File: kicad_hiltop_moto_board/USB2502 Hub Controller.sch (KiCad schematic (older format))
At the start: 39 parts, among them U27 USB2502, U7 AT24C02C-SSHM-T, Y1 50ppm 24.000MHZ

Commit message: Unused pind removed from moto board
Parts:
- U27: symbol Motor_Control_Board-rescue:USB2502-Devtank-Sensi_Board-rescue -> moto_board-rescue:USB2502-Devtank-Sensi_Board-rescue-Motor_Control_Board-rescue
- U7: symbol Motor_Control_Board-rescue:AT24C02C-SSHM-T-Devtank-Sensi_Board-rescue -> moto_board-rescue:AT24C02C-SSHM-T-Devtank-Sensi_Board-rescue-Motor_Control_Board-rescue
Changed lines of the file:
@@
 EESchema Schematic File Version 4
-LIBS:Motor_Control_Board-cache
+LIBS:moto_board-cache
 EELAYER 30 0
 EELAYER END
@@
 $EndDescr
 $Comp
-L Motor_Control_Board-rescue:USB2502-Devtank-Sensi_Board-rescue U27
+L moto_board-rescue:USB2502-Devtank-Sensi_Board-rescue-Motor_Control_Board-rescue U27
 U 1 1 5D8D0F87
 P 6150 4500
@@
 NoConn ~ 5150 3600
 $Comp
-L Motor_Control_Board-rescue:AT24C02C-SSHM-T-Devtank-Sensi_Board-rescue U7
+L moto_board-rescue:AT24C02C-SSHM-T-Devtank-Sensi_Board-rescue-Motor_Control_Board-rescue U7
 U 1 1 5D7EF6D2
 P 9350 5700
+AR Path="/5D7EF6D2" Ref="U7"  Part="1"
+AR Path="/5D8D08E6/5D7EF6D2" Ref="U7"  Part="1"
 F 0 "U7" H 9375 6187 60  0000 C CNN
 F 1 "AT24C02C-SSHM-T" H 9375 6081 60  0000 C CNN

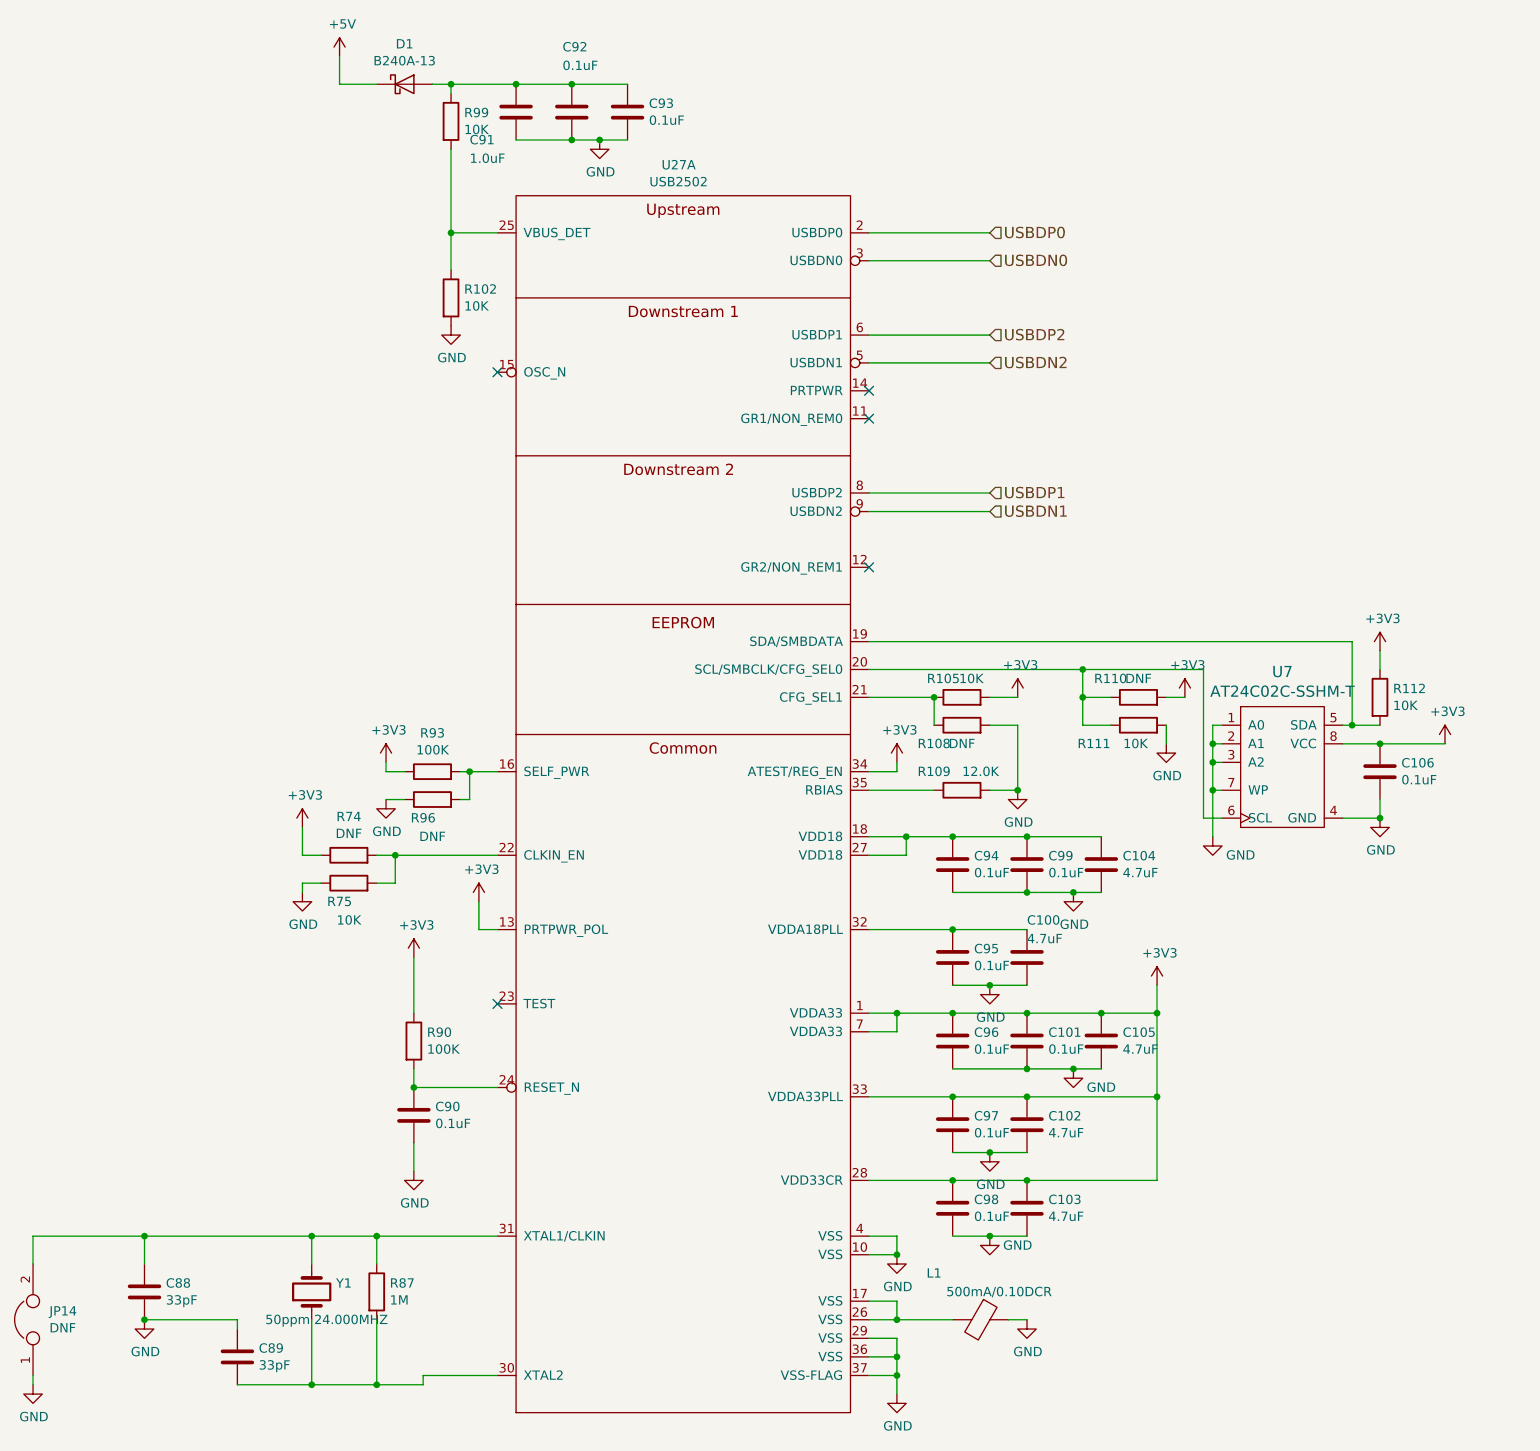
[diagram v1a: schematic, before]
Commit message: Rough layout of moto board
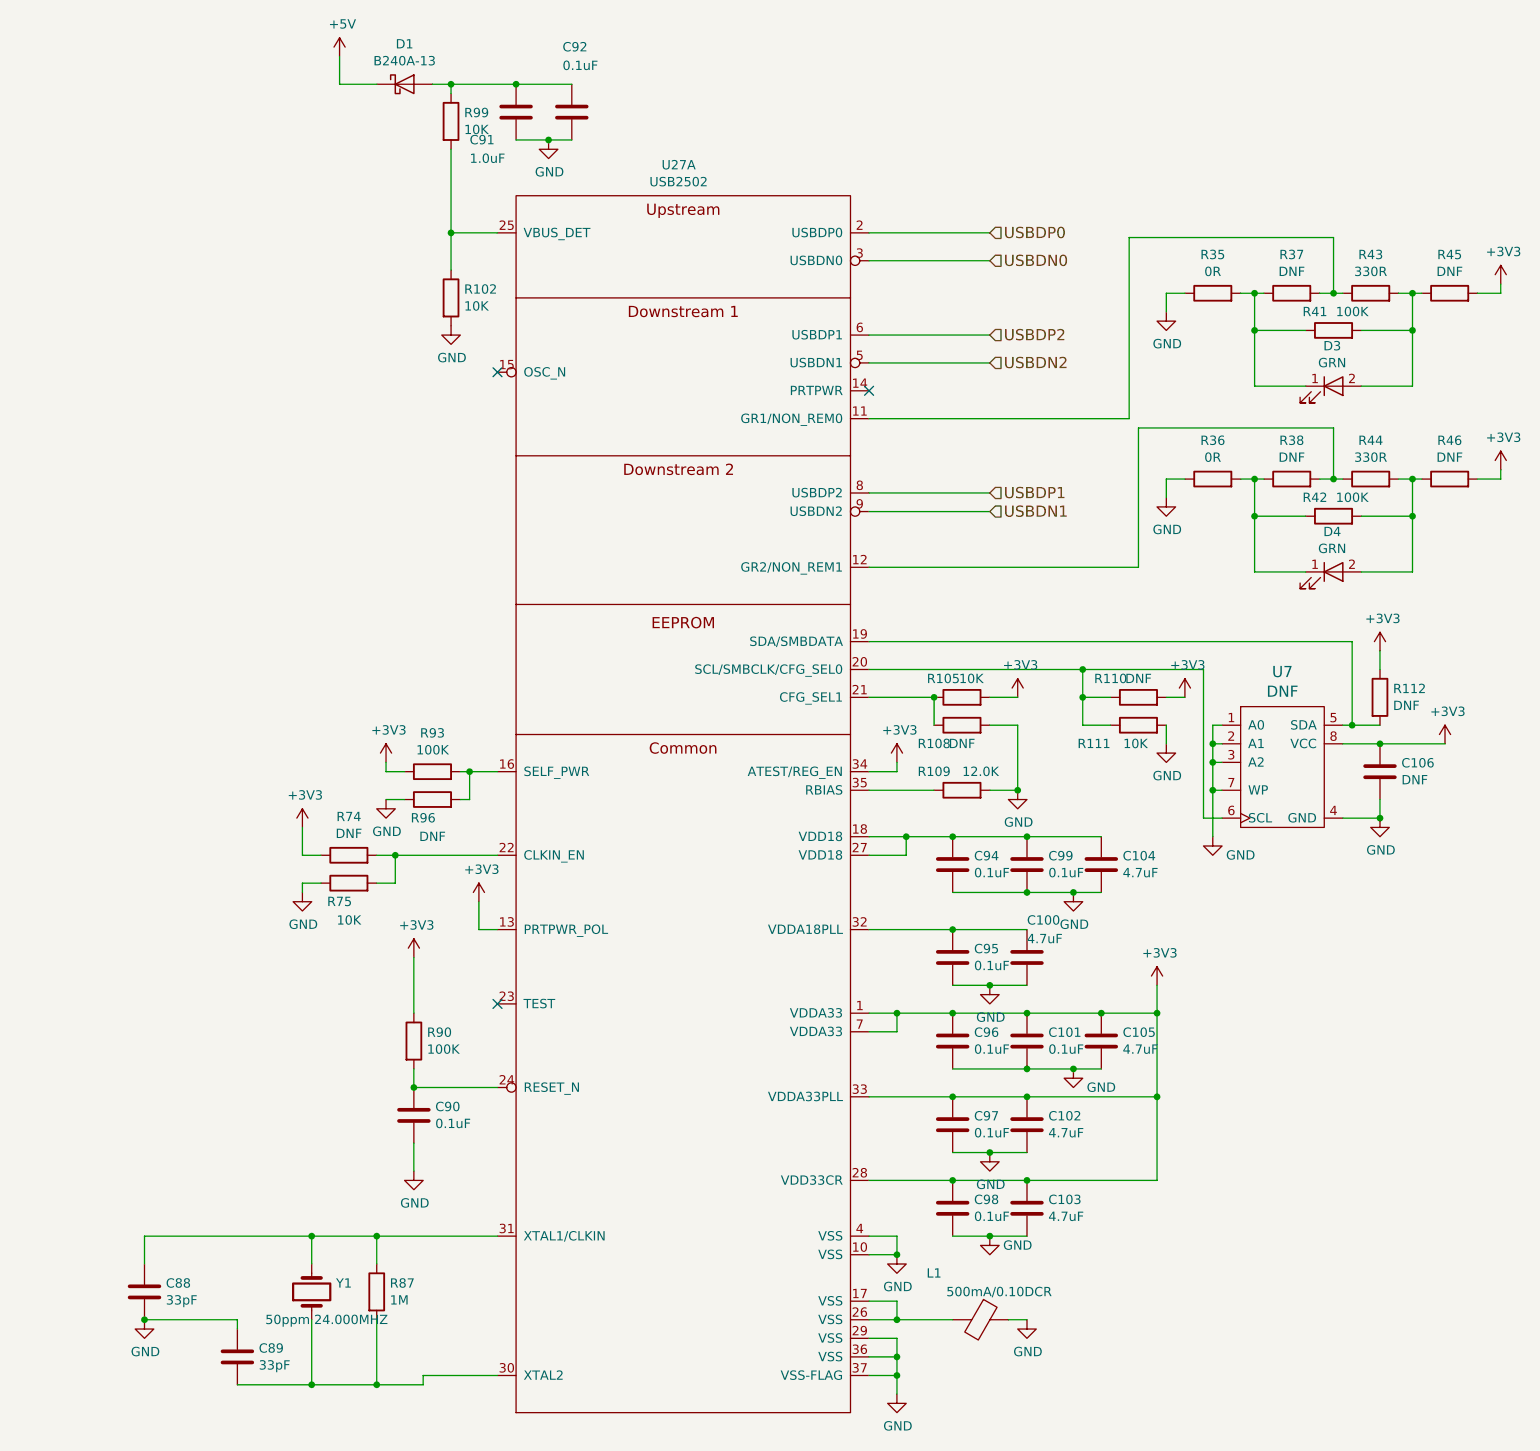
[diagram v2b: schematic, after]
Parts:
- removed C93: 0.1uF, Capacitor_SMD:C_0402_1005Metric, symbol device:C
- removed JP14: DNF, Connector_PinHeader_2.54mm:PinHeader_1x02_P2.54mm_Vertical, symbol device:Jumper
- added D3, D4: GRN, LED_SMD:LED_0603_1608Metric, symbol device:LED
- added R35, R36: 0R, Resistor_SMD:R_0603_1608Metric, symbol device:R
- added R37, R38, R45, R46: DNF, Resistor_SMD:R_0603_1608Metric, symbol device:R
- added R41, R42: 100K, Resistor_SMD:R_0603_1608Metric, symbol device:R
- added R43, R44: 330R, Resistor_SMD:R_0603_1608Metric, symbol device:R
- C106: value 0.1uF -> DNF
- R112: value 10K -> DNF
- U7: value AT24C02C-SSHM-T -> DNF
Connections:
- net +3V3: now also R45.2, R46.2
- net GND: now also R35.1, R36.1
- net at U27.11 (GR1/NON_REM0): now also R37.2, R43.1
- net at U27.12 (GR2/NON_REM1): now also R38.2, R44.1
- new net: D4.1 (K), R36.2, R38.1, R42.1
- new net: D4.2 (A), R42.2, R44.2, R46.1
- new net: D3.1 (K), R35.2, R37.1, R41.1
- new net: D3.2 (A), R41.2, R43.2, R45.1
- no-connect marks 5 -> 3

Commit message: Moto board awaiting review
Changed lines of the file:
@@
 P 4150 8550
 F 0 "Y1" V 4196 8419 50  0000 R CNN
-F 1 "50ppm 24.000MHZ" V 4000 8800 50  0000 R CNN
+F 1 "50ppm 24.000MHZ" V 3975 8900 50  0000 R CNN
 F 2 "Crystal:Crystal_SMD_TXC_7A-2Pin_5x3.2mm" H 4150 8550 50  0001 C CNN
 F 3 "" H 4150 8550 50  0001 C CNN
@@
 U 1 1 5D8F3D03
 P 7650 5500
-F 0 "R108" V 7550 5650 50  0000 C CNN
-F 1 "DNF" V 7550 5500 50  0000 C CNN
+F 0 "R108" V 7550 5600 50  0000 C CNN
+F 1 "DNF" V 7550 5375 50  0000 C CNN
 F 2 "Resistor_SMD:R_0603_1608Metric" V 7580 5500 50  0001 C CNN
 F 3 "" H 7650 5500 50  0001 C CNN
@@
 U 1 1 5D909BDF
 P 8000 7200
-F 0 "C101" H 8115 7246 50  0000 L CNN
-F 1 "0.1uF" H 8115 7155 50  0000 L CNN
+F 0 "C101" H 8100 7250 50  0000 L CNN
+F 1 "0.1uF" H 8100 7150 50  0000 L CNN
 F 2 "Capacitor_SMD:C_0402_1005Metric" H 8038 7050 50  0001 C CNN
 F 3 "" H 8000 7200 50  0001 C CNN
@@
 U 1 1 5D909BE5
 P 8400 7200
-F 0 "C105" H 8515 7246 50  0000 L CNN
-F 1 "4.7uF " H 8515 7155 50  0000 L CNN
+F 0 "C105" H 8500 7225 50  0000 L CNN
+F 1 "4.7uF " H 8475 7125 50  0000 L CNN
 F 2 "Capacitor_SMD:C_0402_1005Metric" H 8438 7050 50  0001 C CNN
 F 3 "" H 8400 7200 50  0001 C CNN
@@
 U 1 1 5D919F57
 P 7600 7650
-F 0 "C97" H 7715 7696 50  0000 L CNN
-F 1 "0.1uF" H 7715 7605 50  0000 L CNN
+F 0 "C97" H 7700 7675 50  0000 L CNN
+F 1 "0.1uF" H 7700 7600 50  0000 L CNN
 F 2 "Capacitor_SMD:C_0402_1005Metric" H 7638 7500 50  0001 C CNN
 F 3 "" H 7600 7650 50  0001 C CNN
@@
 U 1 1 5D929924
 P 7600 6750
-F 0 "C95" H 7715 6796 50  0000 L CNN
-F 1 "0.1uF" H 7715 6705 50  0000 L CNN
+F 0 "C95" H 7700 6800 50  0000 L CNN
+F 1 "0.1uF" H 7700 6700 50  0000 L CNN
 F 2 "Capacitor_SMD:C_0402_1005Metric" H 7638 6600 50  0001 C CNN
 F 3 "" H 7600 6750 50  0001 C CNN
@@
 U 1 1 5D92992A
 P 8000 6750
-F 0 "C100" H 8000 6950 50  0000 L CNN
-F 1 "4.7uF " H 8000 6850 50  0000 L CNN
+F 0 "C100" H 8125 6800 50  0000 L CNN
+F 1 "4.7uF " H 8125 6700 50  0000 L CNN
 F 2 "Capacitor_SMD:C_0402_1005Metric" H 8038 6600 50  0001 C CNN
 F 3 "" H 8000 6750 50  0001 C CNN
@@
 U 1 1 5D938ADF
 P 8000 6250
-F 0 "C99" H 8115 6296 50  0000 L CNN
-F 1 "0.1uF" H 8115 6205 50  0000 L CNN
+F 0 "C99" H 8100 6300 50  0000 L CNN
+F 1 "0.1uF" H 8100 6200 50  0000 L CNN
 F 2 "Capacitor_SMD:C_0402_1005Metric" H 8038 6100 50  0001 C CNN
 F 3 "" H 8000 6250 50  0001 C CNN
@@
 U 1 1 5D938AEB
 P 7600 6250
-F 0 "C94" H 7715 6296 50  0000 L CNN
-F 1 "0.1uF" H 7715 6205 50  0000 L CNN
+F 0 "C94" H 7700 6300 50  0000 L CNN
+F 1 "0.1uF" H 7700 6200 50  0000 L CNN
 F 2 "Capacitor_SMD:C_0402_1005Metric" H 7638 6100 50  0001 C CNN
 F 3 "" H 7600 6250 50  0001 C CNN
@@
 U 1 1 5D947DA8
 P 7650 5350
-F 0 "R105" V 7750 5450 50  0000 C CNN
-F 1 "10K" V 7750 5300 50  0000 C CNN
+F 0 "R105" V 7725 5450 50  0000 C CNN
+F 1 "10K" V 7725 5250 50  0000 C CNN
 F 2 "Resistor_SMD:R_0603_1608Metric" V 7580 5350 50  0001 C CNN
 F 3 "" H 7650 5350 50  0001 C CNN
@@
 U 1 1 5D949CAE
 P 8600 5350
-F 0 "R110" V 8700 5500 50  0000 C CNN
-F 1 "DNF" V 8700 5350 50  0000 C CNN
+F 0 "R110" V 8675 5475 50  0000 C CNN
+F 1 "DNF" V 8675 5250 50  0000 C CNN
 F 2 "Resistor_SMD:R_0603_1608Metric" V 8530 5350 50  0001 C CNN
 F 3 "" H 8600 5350 50  0001 C CNN
@@
 P 8250 6400
 F 0 "#PWR0208" H 8250 6150 50  0001 C CNN
-F 1 "GND" H 8255 6227 50  0000 C CNN
+F 1 "GND" H 8375 6300 50  0000 C CNN
 F 2 "" H 8250 6400 50  0001 C CNN
 F 3 "" H 8250 6400 50  0001 C CNN
@@
 U 1 1 5D9DC3FF
 P 4350 6350
-F 0 "R75" V 4250 6400 50  0000 C CNN
+F 0 "R75" V 4250 6375 50  0000 C CNN
 F 1 "10K " V 4150 6350 50  0000 C CNN
 F 2 "Resistor_SMD:R_0603_1608Metric" V 4280 6350 50  0001 C CNN
@@
 U 1 1 5D9E4A4E
 P 4800 5900
-F 0 "R96" V 4700 5950 50  0000 C CNN
+F 0 "R96" V 4700 5900 50  0000 C CNN
 F 1 "DNF" V 4600 5900 50  0000 C CNN
 F 2 "Resistor_SMD:R_0603_1608Metric" V 4730 5900 50  0001 C CNN
@@
 U 1 1 5D94B078
 P 7650 5850
-F 0 "R109" V 7750 6000 50  0000 C CNN
-F 1 "12.0K " V 7750 5750 50  0000 C CNN
+F 0 "R109" V 7725 6000 50  0000 C CNN
+F 1 "12.0K " V 7725 5725 50  0000 C CNN
 F 2 "Resistor_SMD:R_0603_1608Metric" V 7580 5850 50  0001 C CNN
 F 3 "" H 7650 5850 50  0001 C CNN
@@
 P 7800 6900
 F 0 "#PWR0217" H 7800 6650 50  0001 C CNN
-F 1 "GND" H 7805 6727 50  0000 C CNN
+F 1 "GND" H 7925 6825 50  0000 C CNN
 F 2 "" H 7800 6900 50  0001 C CNN
 F 3 "" H 7800 6900 50  0001 C CNN
@@
 P 7800 7800
 F 0 "#PWR0219" H 7800 7550 50  0001 C CNN
-F 1 "GND" H 7805 7627 50  0000 C CNN
+F 1 "GND" H 7950 7725 50  0000 C CNN
 F 2 "" H 7800 7800 50  0001 C CNN
 F 3 "" H 7800 7800 50  0001 C CNN
@@
 U 1 1 5D8FF0CE
 P 7600 8100
-F 0 "C98" H 7715 8146 50  0000 L CNN
-F 1 "0.1uF" H 7715 8055 50  0000 L CNN
+F 0 "C98" H 7700 8150 50  0000 L CNN
+F 1 "0.1uF" H 7700 8050 50  0000 L CNN
 F 2 "Capacitor_SMD:C_0402_1005Metric" H 7638 7950 50  0001 C CNN
 F 3 "" H 7600 8100 50  0001 C CNN
@@
 U 1 1 5DCA03F2
 P 5250 2200
-F 0 "C91" H 5000 2050 50  0000 L CNN
-F 1 "1.0uF " H 5000 1950 50  0000 L CNN
+F 0 "C91" H 5150 2525 50  0000 L CNN
+F 1 "1.0uF " H 5150 2425 50  0000 L CNN
 F 2 "Capacitor_SMD:C_0402_1005Metric" H 5288 2050 50  0001 C CNN
 F 3 "" H 5250 2200 50  0001 C CNN
@@
 U 1 1 5DCA2D03
 P 5550 2200
-F 0 "C92" H 5500 2550 50  0000 L CNN
-F 1 "0.1uF" H 5500 2450 50  0000 L CNN
+F 0 "C92" H 5475 2475 50  0000 L CNN
+F 1 "0.1uF" H 5475 2400 50  0000 L CNN
 F 2 "Capacitor_SMD:C_0402_1005Metric" H 5588 2050 50  0001 C CNN
 F 3 "" H 5550 2200 50  0001 C CNN
@@
 AR Path="/5D8D08E6/5E674F93" Ref="#PWR0202"  Part="1"
 F 0 "#PWR0202" H 7950 5200 50  0001 C CNN
-F 1 "+3V3" H 7965 5523 50  0000 C CNN
+F 1 "+3V3" H 8075 5450 50  0000 C CNN
 F 2 "" H 7950 5350 50  0001 C CNN
 F 3 "" H 7950 5350 50  0001 C CNN

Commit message: added bom
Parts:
- C106: Devtank 105-019 -> (none)
- D3, D4: Devtank (none) -> 110-002
- L1: Devtank (none) -> 113-004
- R112: Devtank 101-010 -> (none)
- R35, R36: Devtank (none) -> 101-005
- R41, R42: Devtank (none) -> 101-015
- R43, R44: Devtank (none) -> 101-024
- U7: Devtank 129-006 -> (none)
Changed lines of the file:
@@
 F 2 "Capacitor_SMD:C_0402_1005Metric" H 9938 5600 50  0001 C CNN
 F 3 "" H 9900 5750 50  0001 C CNN
-F 4 "105-019" H 9900 5750 50  0001 C CNN "Devtank"
+F 4 "" H 9900 5750 50  0001 C CNN "Devtank"
 	1    9900 5750
 	1    0    0    -1
@@
 F 2 "Resistor_SMD:R_0603_1608Metric" V 9830 5350 50  0001 C CNN
 F 3 "" H 9900 5350 50  0001 C CNN
-F 4 "101-010" H 9900 5350 50  0001 C CNN "Devtank"
+F 4 "" H 9900 5350 50  0001 C CNN "Devtank"
 	1    9900 5350
 	1    0    0    -1
@@
 F 2 "Inductor_SMD:L_0805_2012Metric" V 7680 8700 50  0001 C CNN
 F 3 "" H 7750 8700 50  0001 C CNN
+F 4 "113-004" H 7750 8700 50  0001 C CNN "Devtank"
 	1    7750 8700
 	0    1    1    0
@@
 F 2 "Package_SO:SOIC-8_3.9x4.9mm_P1.27mm" H 9300 5150 60  0001 C CNN
 F 3 "" H 9300 5150 60  0001 C CNN
-F 4 "129-006" H 9350 5700 50  0001 C CNN "Devtank"
+F 4 "" H 9350 5700 50  0001 C CNN "Devtank"
 	1    9350 5700
 	1    0    0    -1
@@
 F 2 "Resistor_SMD:R_0603_1608Metric" V 8930 4175 50  0001 C CNN
 F 3 "" H 9000 4175 50  0001 C CNN
+F 4 "101-005" H 9000 4175 50  0001 C CNN "Devtank"
 	1    9000 4175
 	0    -1   -1   0
@@
 F 2 "Resistor_SMD:R_0603_1608Metric" V 9780 4175 50  0001 C CNN
 F 3 "" H 9850 4175 50  0001 C CNN
+F 4 "101-024" H 9850 4175 50  0001 C CNN "Devtank"
 	1    9850 4175
 	0    -1   -1   0
@@
 F 2 "Resistor_SMD:R_0603_1608Metric" V 9580 4375 50  0001 C CNN
 F 3 "" H 9650 4375 50  0001 C CNN
+F 4 "101-015" H 9650 4375 50  0001 C CNN "Devtank"
 	1    9650 4375
 	0    -1   -1   0
@@
 F 2 "LED_SMD:LED_0603_1608Metric" H 9650 4675 50  0001 C CNN
 F 3 "~" H 9650 4675 50  0001 C CNN
+F 4 "110-002" H 9650 4675 50  0001 C CNN "Devtank"
 	1    9650 4675
 	1    0    0    -1
@@
 F 2 "Resistor_SMD:R_0603_1608Metric" V 8930 3175 50  0001 C CNN
 F 3 "" H 9000 3175 50  0001 C CNN
+F 4 "101-005" H 9000 3175 50  0001 C CNN "Devtank"
 	1    9000 3175
 	0    -1   -1   0
@@
 F 2 "Resistor_SMD:R_0603_1608Metric" V 9780 3175 50  0001 C CNN
 F 3 "" H 9850 3175 50  0001 C CNN
+F 4 "101-024" H 9850 3175 50  0001 C CNN "Devtank"
 	1    9850 3175
 	0    -1   -1   0
@@
 F 2 "Resistor_SMD:R_0603_1608Metric" V 9580 3375 50  0001 C CNN
 F 3 "" H 9650 3375 50  0001 C CNN
+F 4 "101-015" H 9650 3375 50  0001 C CNN "Devtank"
 	1    9650 3375
 	0    -1   -1   0
@@
 F 2 "LED_SMD:LED_0603_1608Metric" H 9650 3675 50  0001 C CNN
 F 3 "~" H 9650 3675 50  0001 C CNN
+F 4 "110-002" H 9650 3675 50  0001 C CNN "Devtank"
 	1    9650 3675
 	1    0    0    -1
